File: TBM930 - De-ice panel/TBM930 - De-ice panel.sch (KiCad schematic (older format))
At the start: 69 parts, among them J1 SW_AIRFRAME_DE_ICE, J10 AVR-ISP-6, J11 Screw_Terminal_01x02, J2 SW_ICE_LIGHT, J3 SW_PROP_DE_ICE, J4 SW_WIND_SHIELD, J5 SW_PITOT_L_HTR, J6 SW_PITOT_R_HTR, J7 SW_INERT_SEP, J8 Barrel_Jack, J9 USB_B_Mini, SW1 SW_Push, SW2 SW_Push, U1 TLC5917IN, U2 TLC5917IN, U3 ATmega32U4-MU, Y1 Crystal_GND24

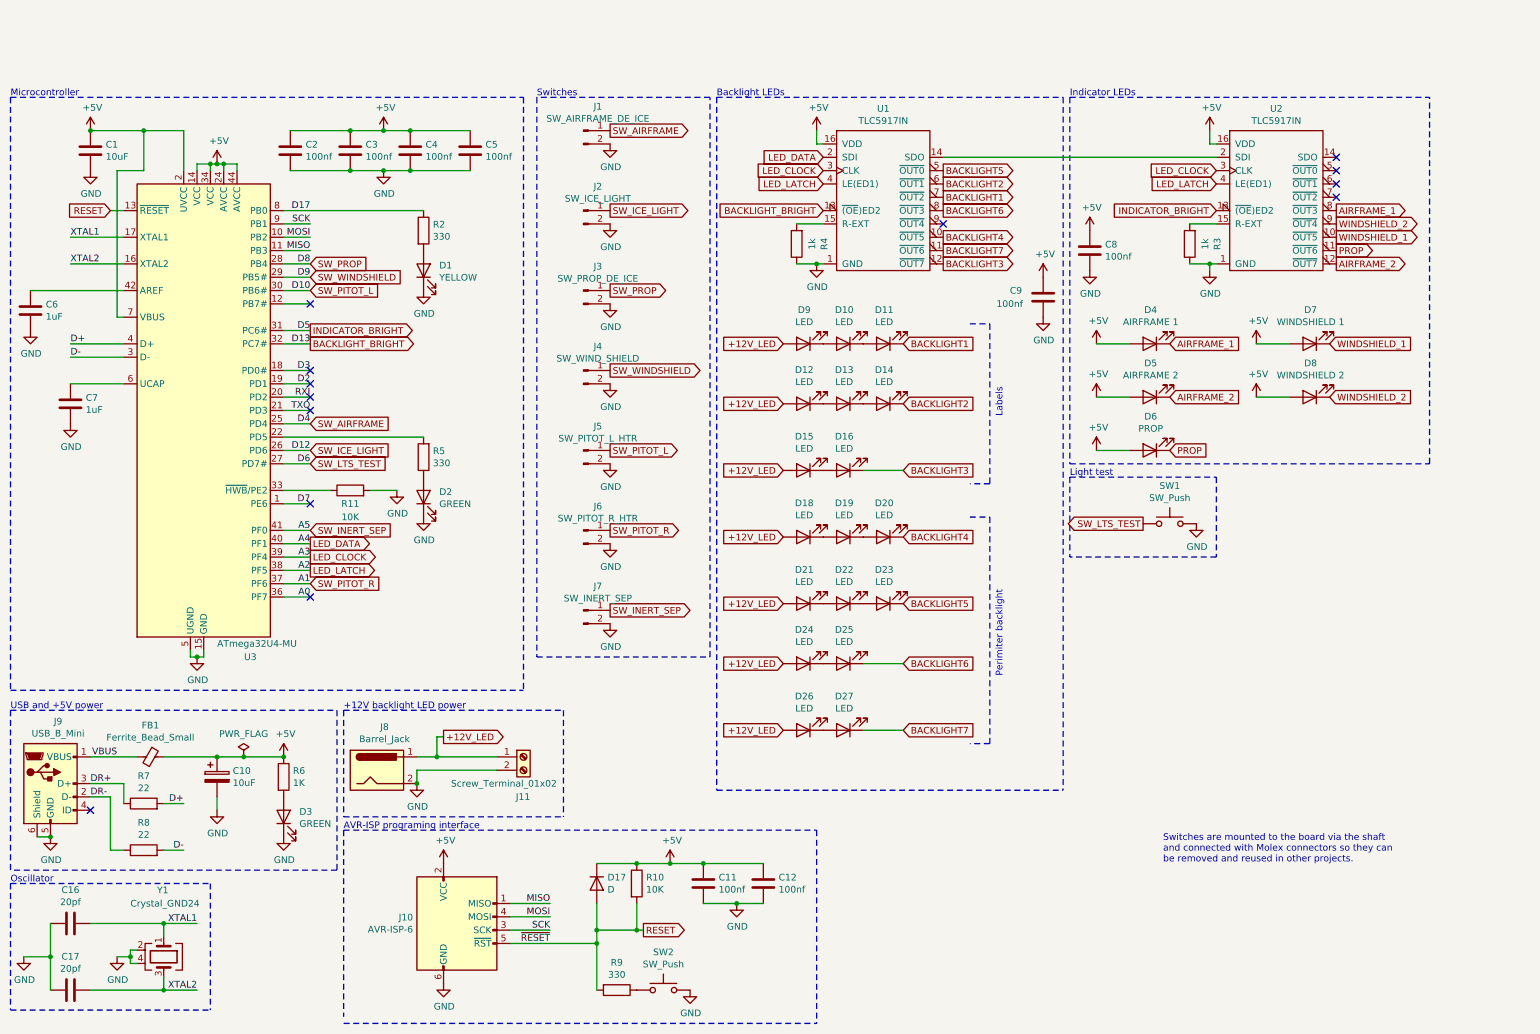
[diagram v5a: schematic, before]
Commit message: Breakout board and tbm930 board updates
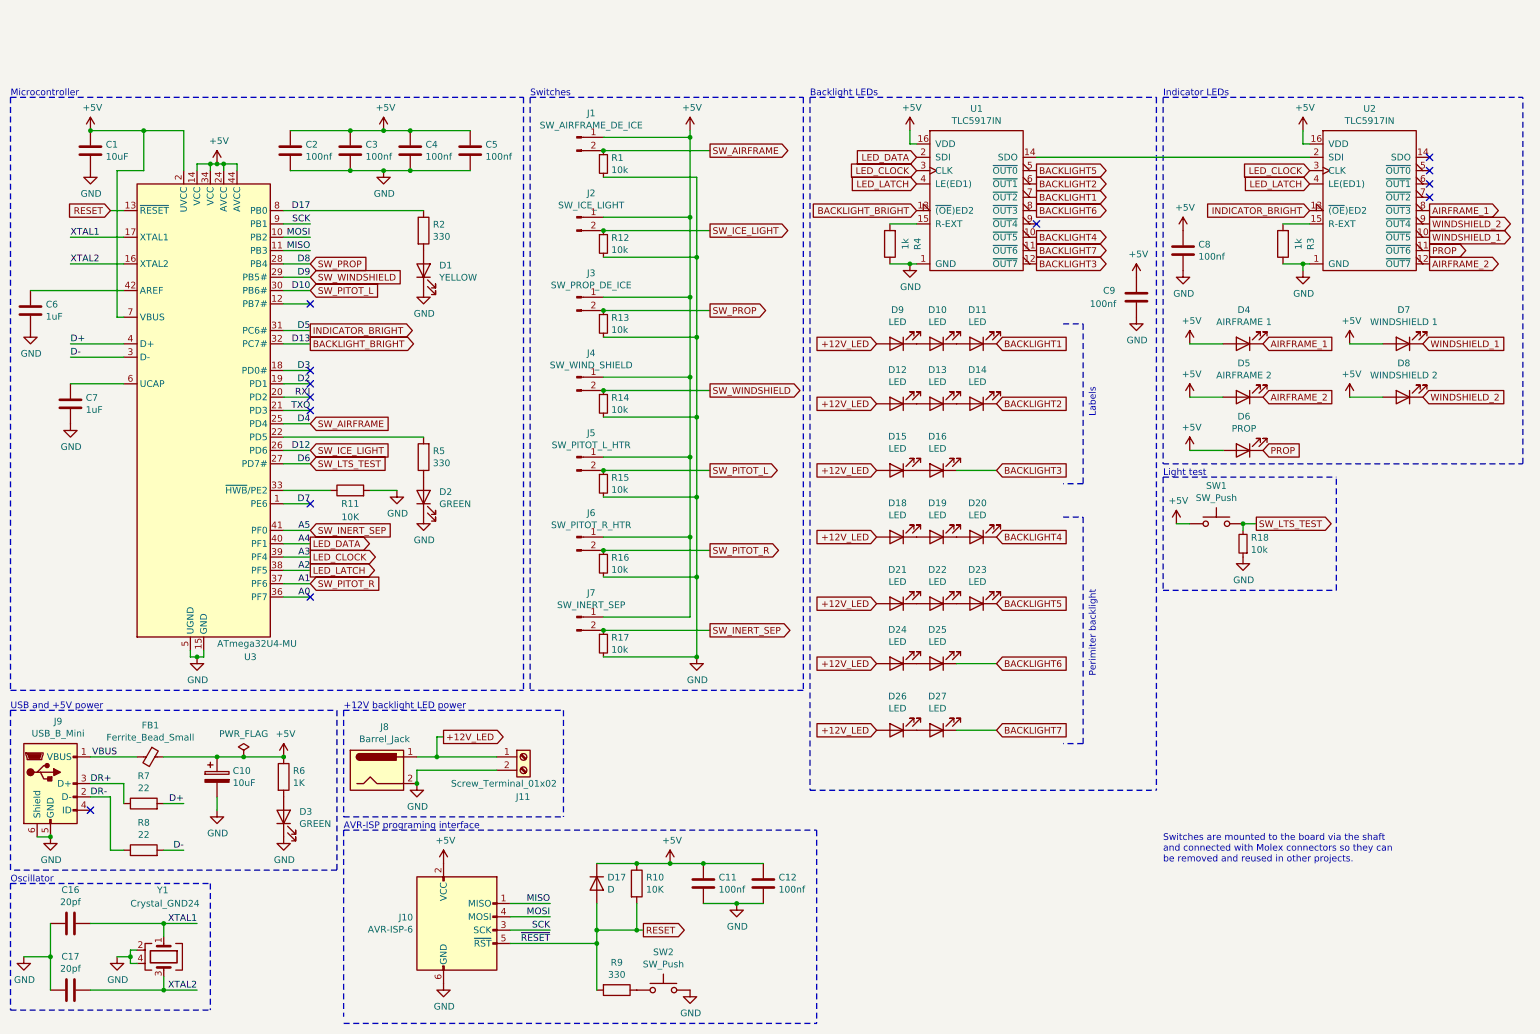
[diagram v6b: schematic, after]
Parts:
- added R1, R12, R13, R14, R15, R16, R17, R18: 10k, Resistor_SMD:R_0402_1005Metric, symbol Device:R_Small
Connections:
- net +5V: now also J1.1 (Pin_1), J2.1 (Pin_1), J3.1 (Pin_1), J4.1 (Pin_1), J5.1 (Pin_1), J6.1 (Pin_1), J7.1 (Pin_1), SW1.1
- net GND: now also R1.2, R12.2, R13.2, R14.2, R15.2, R16.2, R17.2, R18.1; no longer J1.2 (Pin_2), J2.2 (Pin_2), J3.2 (Pin_2), J4.2 (Pin_2), J5.2 (Pin_2), J6.2 (Pin_2), J7.2 (Pin_2), SW1.2
- net SW_AIRFRAME: now also J1.2 (Pin_2), R1.1; no longer J1.1 (Pin_1)
- net SW_ICE_LIGHT: now also J2.2 (Pin_2), R12.1; no longer J2.1 (Pin_1)
- net SW_INERT_SEP: now also J7.2 (Pin_2), R17.1; no longer J7.1 (Pin_1)
- net SW_LTS_TEST: now also SW1.2, R18.2; no longer SW1.1
- net SW_PITOT_L: now also J5.2 (Pin_2), R15.1; no longer J5.1 (Pin_1)
- net SW_PITOT_R: now also J6.2 (Pin_2), R16.1; no longer J6.1 (Pin_1)
- net SW_PROP: now also J3.2 (Pin_2), R13.1; no longer J3.1 (Pin_1)
- net SW_WINDSHIELD: now also J4.2 (Pin_2), R14.1; no longer J4.1 (Pin_1)
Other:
- moved on the sheet: C8, C9, D10, D11, D12, D13, D14, D15, D16, D18, D19, D20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

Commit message: Cleanup references so it should open on any machine
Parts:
- C1, C11, C12, C16, C17, C2, C3, C4, C5, C6, C7, C8, C9: symbol Device:C -> Device:C_Small
- C10: symbol Device:CP -> Device:CP_Small
- D1, D2, D3: footprint Global MobiFlight panel parts:LED_0603_1608Metric -> TBM930 - De-ice panel:LED_0603_1608Metric; symbol Device:LED -> Device:LED_Small
- D10, D11, D12, D13, D14, D15, D16, D18, D19, D20, D21, D22, D23, D24, D25, D26, D27, D9: footprint Global MobiFlight panel parts:LED_1206_3216Metric_Pad1.42x1.75mm_HandSolder -> TBM930 - De-ice panel:LED_1206_3216Metric_Pad1.42x1.75mm_HandSolder
- D17: symbol Device:D -> Device:D_Small
- J8: footprint Global MobiFlight panel parts:BarrelJack_Horizontal -> TBM930 - De-ice panel:BarrelJack_Horizontal
- J9: footprint Global MobiFlight panel parts:USB_B_Mini_Amphenol_UE25BE5510H -> TBM930 - De-ice panel:USB_B_Mini_Amphenol_UE25BE5510H
- R10, R11, R2, R3, R4, R5, R6, R7, R8, R9: symbol Device:R -> Device:R_Small
- U1, U2: symbol Global_MobiFlight_panel_parts:TLC5917IN -> TBM930_De-ice_panel:TLC5917IN
- U3: symbol Global_MobiFlight_panel_parts:ATmega32U4-MU -> TBM930_De-ice_panel:ATmega16U4-MU-Exposed-Extra-Pins
- Y1: symbol Global_MobiFlight_panel_parts:Crystal_GND24 -> TBM930_De-ice_panel:Crystal_GND24
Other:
- moved on the sheet: C1, C11, C12, C16, C17, C6, C7, D1, D17, D2, D3, R10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
